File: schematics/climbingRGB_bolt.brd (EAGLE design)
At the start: 38.1 x 15.9 mm, 3 parts

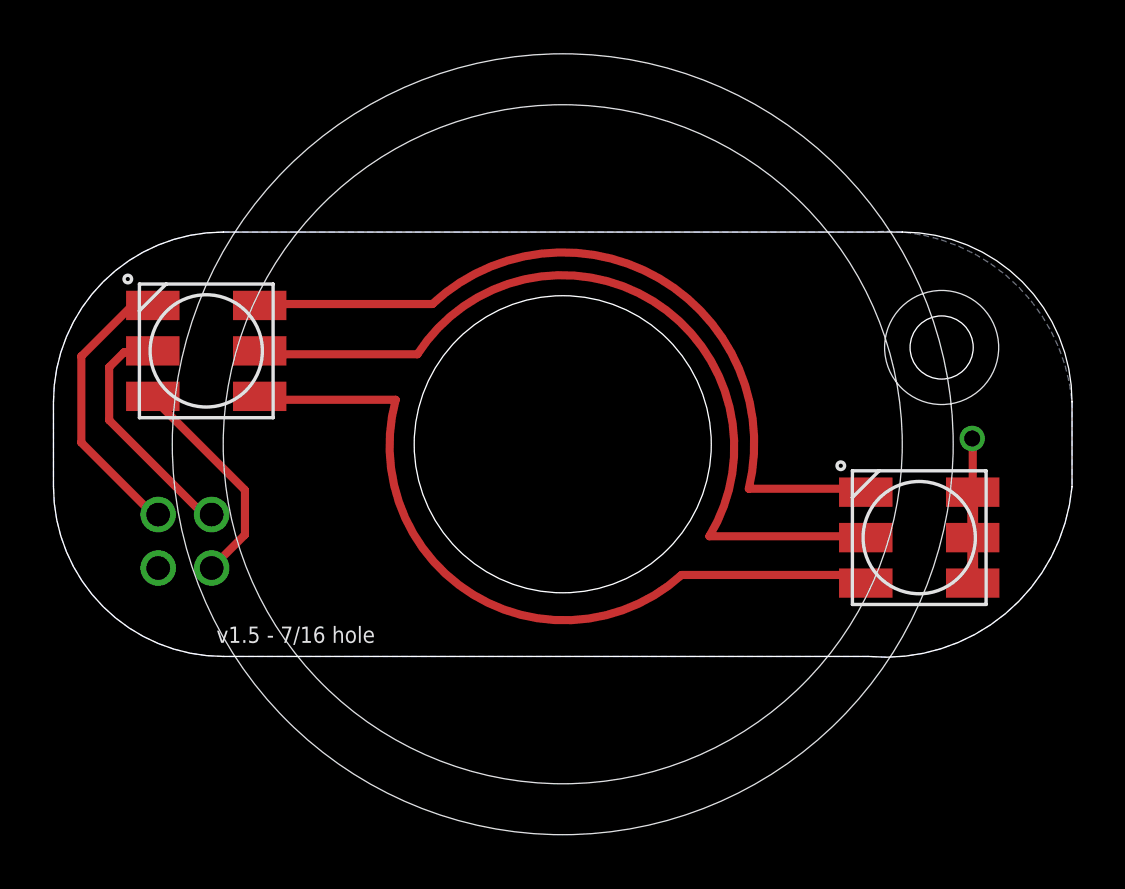
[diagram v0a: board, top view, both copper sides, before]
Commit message: changed WS2812 controller to uUSB, minor spacing edits to everything else
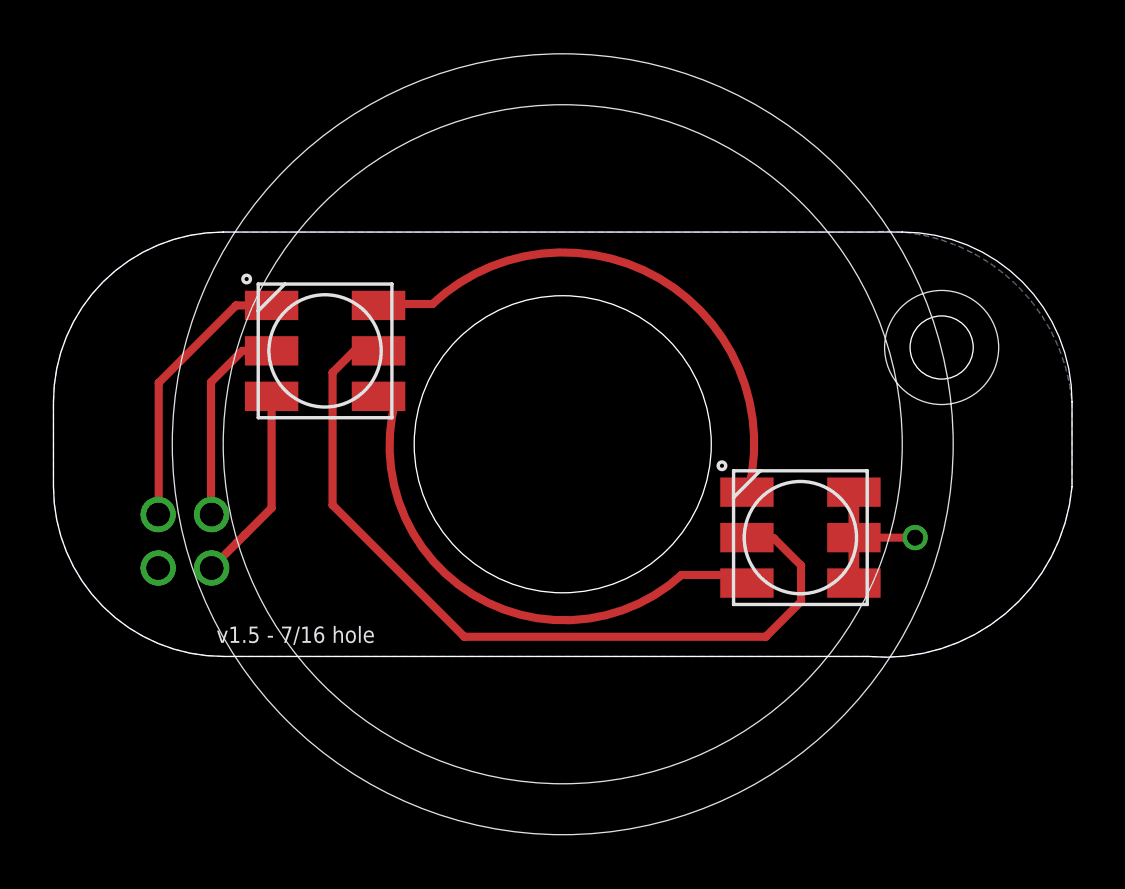
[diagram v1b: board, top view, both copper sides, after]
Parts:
- moved LED4 4.45 mm to (10.2, 11.4)
- moved LED3 4.44 mm to (27.9, 4.45)
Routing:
- net N$5: track 24.7 -> 15.8 mm
- net N$1: track 24.6 -> 15.9 mm
- net N$6: track 24.7 -> 30.9 mm
- net RED: track 9.16 -> 7.71 mm
- net GREEN: track 8.37 -> 7.35 mm
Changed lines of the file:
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@@
 </autorouter>
 <elements>
-<element name="LED3" library="adafruit" package="RGBLED5050" value="RGBLED5050" x="32.385" y="4.445" smashed="yes" rot="R180"/>
-<element name="LED4" library="adafruit" package="RGBLED5050" value="RGBLED5050" x="5.715" y="11.43" smashed="yes" rot="R180"/>
+<element name="LED3" library="adafruit" package="RGBLED5050" value="RGBLED5050" x="27.94" y="4.445" smashed="yes" rot="R180"/>
+<element name="LED4" library="adafruit" package="RGBLED5050" value="RGBLED5050" x="10.16" y="11.43" smashed="yes" rot="R180"/>
 <element name="U$1" library="SparkFun-Connectors" package="SWR204" value="SWR204-D02" x="4.8768" y="4.318" rot="MR270"/>
 </elements>
@@
 <contactref element="LED4" pad="3"/>
 <wire x1="14.1732" y1="13.1826" x2="26.0096" y2="6.2738" width="0.3048" layer="1" curve="-146.795156"/>
-<wire x1="14.1732" y1="13.1826" x2="7.7676" y2="13.1826" width="0.3048" layer="1"/>
-<wire x1="7.7676" y1="13.1826" x2="7.715" y2="13.13" width="0.3048" layer="1"/>
-<wire x1="26.0096" y1="6.2738" x2="30.2562" y2="6.2738" width="0.3048" layer="1"/>
-<wire x1="30.2562" y1="6.2738" x2="30.385" y2="6.145" width="0.3048" layer="1"/>
+<wire x1="14.1732" y1="13.1826" x2="12.2126" y2="13.1826" width="0.3048" layer="1"/>
+<wire x1="12.2126" y1="13.1826" x2="12.16" y2="13.13" width="0.3048" layer="1"/>
+<wire x1="26.0096" y1="6.2738" x2="26.0096" y2="6.2146" width="0.3048" layer="1"/>
+<wire x1="26.0096" y1="6.2146" x2="25.94" y2="6.145" width="0.3048" layer="1"/>
 </signal>
 <signal name="N$5">
@@
 <contactref element="LED4" pad="1"/>
 <wire x1="23.495" y1="3.048" x2="12.8016" y2="9.6012" width="0.3048" layer="1" curve="-147.469526"/>
-<wire x1="12.8016" y1="9.6012" x2="7.8438" y2="9.6012" width="0.3048" layer="1"/>
-<wire x1="7.8438" y1="9.6012" x2="7.715" y2="9.73" width="0.3048" layer="1"/>
-<wire x1="23.495" y1="3.048" x2="30.082" y2="3.048" width="0.3048" layer="1"/>
-<wire x1="30.082" y1="3.048" x2="30.385" y2="2.745" width="0.3048" layer="1"/>
+<wire x1="12.8016" y1="9.6012" x2="12.2888" y2="9.6012" width="0.3048" layer="1"/>
+<wire x1="12.2888" y1="9.6012" x2="12.16" y2="9.73" width="0.3048" layer="1"/>
+<wire x1="23.495" y1="3.048" x2="25.637" y2="3.048" width="0.3048" layer="1"/>
+<wire x1="25.637" y1="3.048" x2="25.94" y2="2.745" width="0.3048" layer="1"/>
 </signal>
 <signal name="N$6">
 <contactref element="LED3" pad="5"/>
 <contactref element="LED4" pad="2"/>
-<wire x1="13.6144" y1="11.303" x2="24.5364" y2="4.4958" width="0.3048" layer="1" curve="-178.4896"/>
-<wire x1="13.6144" y1="11.303" x2="7.842" y2="11.303" width="0.3048" layer="1"/>
-<wire x1="7.842" y1="11.303" x2="7.715" y2="11.43" width="0.3048" layer="1"/>
-<wire x1="24.5364" y1="4.4958" x2="30.3342" y2="4.4958" width="0.3048" layer="1"/>
-<wire x1="30.3342" y1="4.4958" x2="30.385" y2="4.445" width="0.3048" layer="1"/>
+<wire x1="12.16" y1="11.43" x2="11.2522" y2="11.43" width="0.3048" layer="1"/>
+<wire x1="11.2522" y1="11.43" x2="10.4394" y2="10.6172" width="0.3048" layer="1"/>
+<wire x1="10.4394" y1="10.6172" x2="10.4394" y2="5.6642" width="0.3048" layer="1"/>
+<wire x1="10.4394" y1="5.6642" x2="15.367" y2="0.7366" width="0.3048" layer="1"/>
+<wire x1="15.367" y1="0.7366" x2="26.6446" y2="0.7366" width="0.3048" layer="1"/>
+<wire x1="26.6446" y1="0.7366" x2="27.9654" y2="2.0574" width="0.3048" layer="1"/>
+<wire x1="27.9654" y1="2.0574" x2="27.9654" y2="3.4036" width="0.3048" layer="1"/>
+<wire x1="27.9654" y1="3.4036" x2="26.9494" y2="4.4196" width="0.3048" layer="1"/>
+<wire x1="26.9494" y1="4.4196" x2="25.9654" y2="4.4196" width="0.3048" layer="1"/>
+<wire x1="25.9654" y1="4.4196" x2="25.94" y2="4.445" width="0.3048" layer="1"/>
 </signal>
 <signal name="VCC">
@@
 <contactref element="LED3" pad="1"/>
 <contactref element="LED3" pad="3"/>
-<wire x1="34.385" y1="6.145" x2="34.385" y2="4.445" width="0.4064" layer="1"/>
-<wire x1="34.385" y1="4.445" x2="34.385" y2="2.745" width="0.4064" layer="1"/>
+<wire x1="29.94" y1="6.145" x2="29.94" y2="4.445" width="0.4064" layer="1"/>
+<wire x1="29.94" y1="4.445" x2="29.94" y2="2.745" width="0.4064" layer="1"/>
 <contactref element="U$1" pad="P$4"/>
 <polygon width="0.8128" layer="16" rank="6">
@@
 <vertex x="30.48" y="15.875" curve="-90"/>
 </polygon>
-<via x="34.3662" y="8.1534" extent="1-16" drill="0.6" shape="octagon"/>
-<wire x1="34.385" y1="6.145" x2="34.385" y2="7.74444375" width="0.3048" layer="1"/>
-<wire x1="34.385" y1="7.74444375" x2="34.3662" y2="8.1534" width="0.3048" layer="1" curve="45"/>
+<via x="32.2326" y="4.445" extent="1-16" drill="0.6" shape="octagon"/>
+<wire x1="32.2326" y1="4.445" x2="29.94" y2="4.445" width="0.3048" layer="1"/>
 </signal>
 <signal name="GREEN">
 <contactref element="LED4" pad="6"/>
 <contactref element="U$1" pad="P$3"/>
-<wire x1="3.715" y1="9.73" x2="3.715" y2="9.6708" width="0.3048" layer="1"/>
-<wire x1="3.715" y1="9.6708" x2="7.1628" y2="6.223" width="0.3048" layer="1"/>
-<wire x1="7.1628" y1="6.223" x2="7.1628" y2="4.554" width="0.3048" layer="1"/>
-<wire x1="7.1628" y1="4.554" x2="5.9168" y2="3.308" width="0.3048" layer="1"/>
+<wire x1="7.1628" y1="4.554" x2="6.867" y2="4.2582" width="0.3048" layer="1"/>
+<wire x1="6.867" y1="4.2582" x2="5.9168" y2="3.308" width="0.3048" layer="1"/>
+<wire x1="8.16" y1="9.73" x2="8.16" y2="5.5512" width="0.3048" layer="1"/>
+<wire x1="8.16" y1="5.5512" x2="7.1628" y2="4.554" width="0.3048" layer="1"/>
 </signal>
 <signal name="BLUE">
 <contactref element="LED4" pad="4"/>
 <contactref element="U$1" pad="P$1"/>
-<wire x1="1.0414" y1="8.001" x2="1.0414" y2="11.2268" width="0.3048" layer="1"/>
-<wire x1="1.0414" y1="11.2268" x2="2.9718" y2="13.1572" width="0.3048" layer="1"/>
-<wire x1="2.9718" y1="13.1572" x2="3.6878" y2="13.1572" width="0.3048" layer="1"/>
-<wire x1="3.6878" y1="13.1572" x2="3.715" y2="13.13" width="0.3048" layer="1"/>
-<wire x1="3.9168" y1="5.308" x2="3.7344" y2="5.308" width="0.3048" layer="1"/>
-<wire x1="3.7344" y1="5.308" x2="1.0414" y2="8.001" width="0.3048" layer="1"/>
+<wire x1="8.16" y1="13.13" x2="6.8308" y2="13.13" width="0.3048" layer="1"/>
+<wire x1="6.8308" y1="13.13" x2="3.937" y2="10.2362" width="0.3048" layer="1"/>
+<wire x1="3.937" y1="10.2362" x2="3.937" y2="5.3282" width="0.3048" layer="1"/>
+<wire x1="3.937" y1="5.3282" x2="3.9168" y2="5.308" width="0.3048" layer="1"/>
 </signal>
 <signal name="RED">
 <contactref element="LED4" pad="5"/>
 <contactref element="U$1" pad="P$2"/>
-<wire x1="2.0828" y1="8.8392" x2="2.0828" y2="10.8204" width="0.3048" layer="1"/>
-<wire x1="2.0828" y1="10.8204" x2="2.6416" y2="11.3792" width="0.3048" layer="1"/>
-<wire x1="2.6416" y1="11.3792" x2="3.6642" y2="11.3792" width="0.3048" layer="1"/>
-<wire x1="3.6642" y1="11.3792" x2="3.715" y2="11.43" width="0.3048" layer="1"/>
-<wire x1="5.9168" y1="5.308" x2="5.614" y2="5.308" width="0.3048" layer="1"/>
-<wire x1="5.614" y1="5.308" x2="2.0828" y2="8.8392" width="0.3048" layer="1"/>
+<wire x1="8.16" y1="11.43" x2="7.0612" y2="11.43" width="0.3048" layer="1"/>
+<wire x1="7.0612" y1="11.43" x2="5.8928" y2="10.2616" width="0.3048" layer="1"/>
+<wire x1="5.8928" y1="10.2616" x2="5.8928" y2="5.332" width="0.3048" layer="1"/>
+<wire x1="5.8928" y1="5.332" x2="5.9168" y2="5.308" width="0.3048" layer="1"/>
 </signal>
 </signals>
